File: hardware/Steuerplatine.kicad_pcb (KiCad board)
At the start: 2 copper layers, 110 x 110 mm, 52 parts, among them J1 Conn_01x02_Pin, J2 Conn_01x02_Pin, Q2 BTA16-600B, Q3 BC847BS, U1 LPS28DFW, U2 LNK3202D, U3 Seeed-ESP32C3, U4 TL082

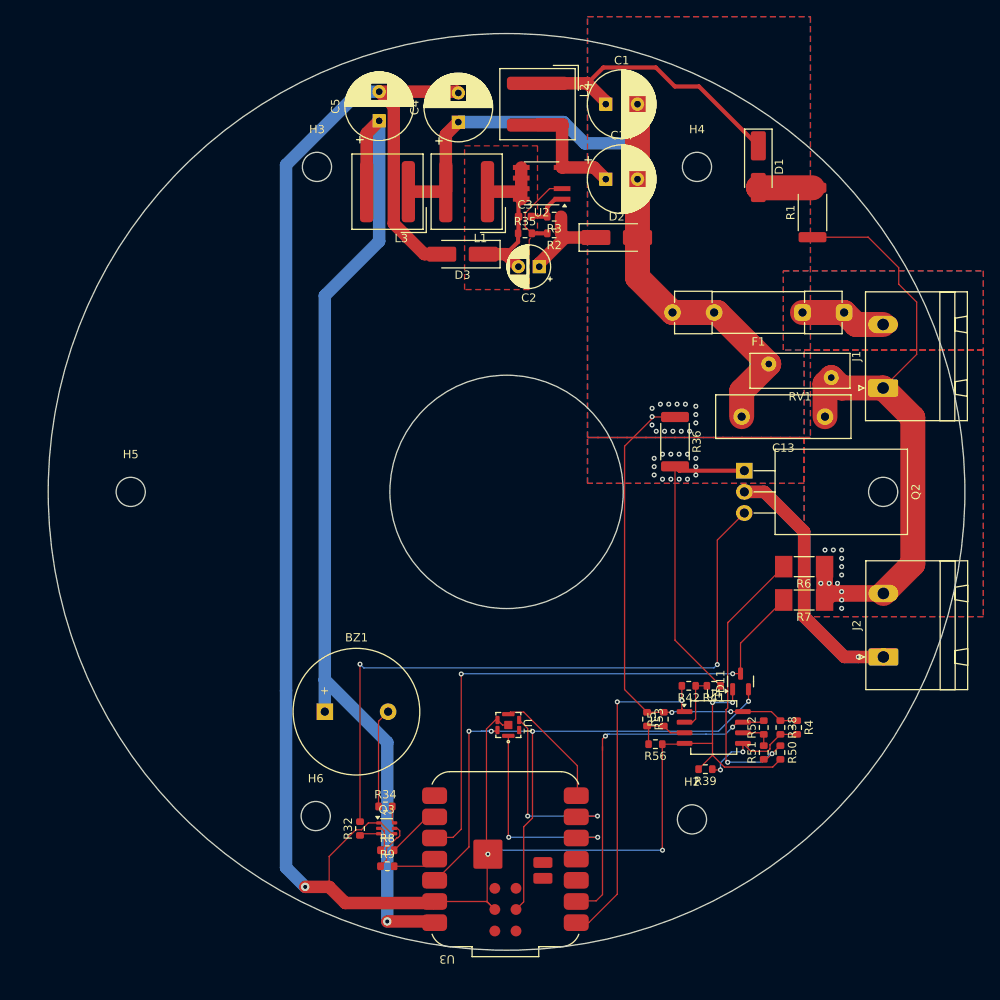
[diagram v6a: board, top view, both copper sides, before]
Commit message: added gnd layer
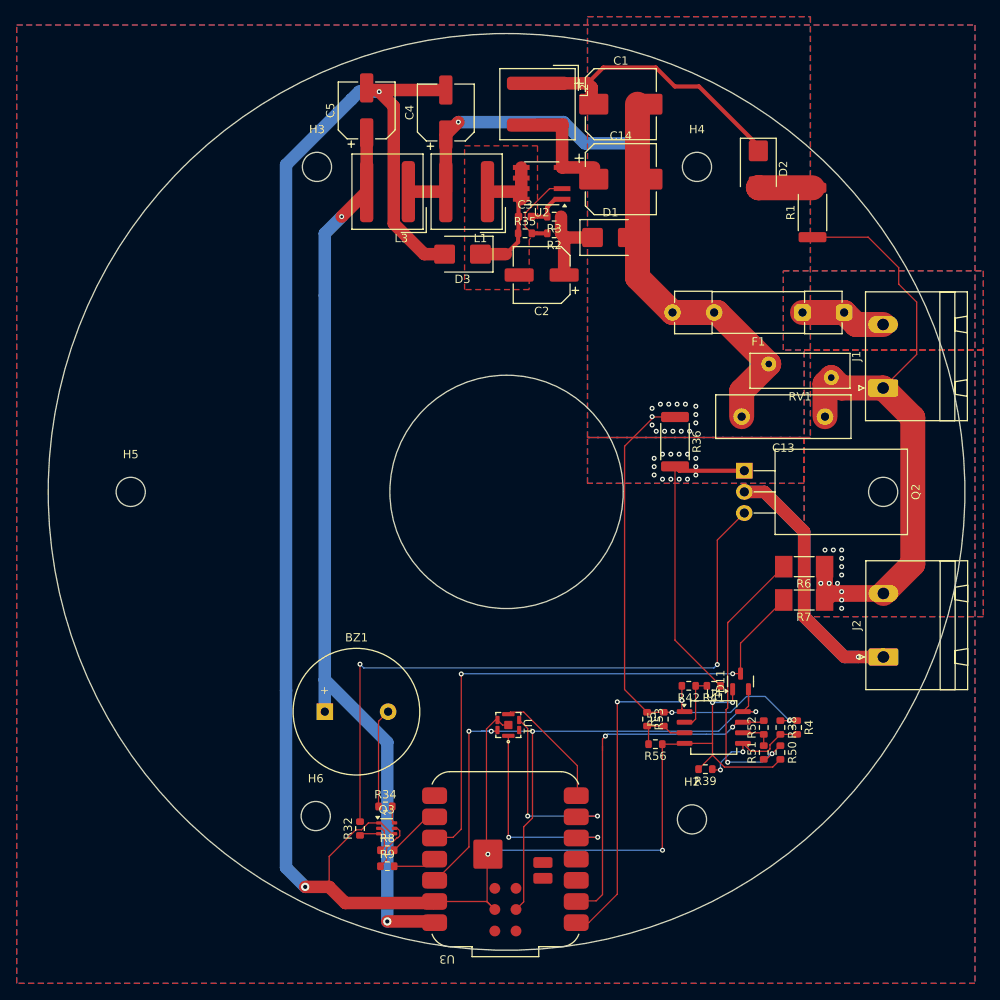
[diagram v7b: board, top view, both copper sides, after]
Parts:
- C1, C14: footprint Capacitor_THT:CP_Radial_D8.0mm_P3.80mm -> Capacitor_SMD:CP_Elec_8x10
- C2: footprint Capacitor_THT:CP_Radial_D5.0mm_P2.50mm -> Capacitor_SMD:CP_Elec_6.3x3
- C4, C5: value 220u -> 22u; footprint Capacitor_THT:CP_Radial_D8.0mm_P3.50mm -> Capacitor_SMD:CP_Elec_6.3x3
- D1: value D -> UF4007; footprint Diode_SMD:D_SMA_Handsoldering -> Diode_SMD:D_SMB
- D2, D3: footprint Diode_SMD:D_SMA_Handsoldering -> Diode_SMD:D_SMB
- moved D1 19.7 mm to (166.2, 110.5), turned to 0 degrees
- moved D2 18.9 mm to (184.0, 102.2), turned to -90 degrees
- moved C5 1.95 mm to (137.0, 95.2)
- moved C4 1.89 mm to (146.5, 95.5)
- moved C1 1.80 mm to (167.5, 94.5)
- moved C14 1.80 mm to (167.5, 103.5)
- moved C2 1.04 mm to (158.0, 115.0)
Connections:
- C1 pad 1: Net-(D1-K) -> Net-(D2-K)
- C2 pad 1: Net-(D2-K) -> Net-(D1-K)
- D1 pad 2: Net-(D1-A) -> /N_filt
- D2 pad 2: /N_filt -> Net-(D2-A)
- L2 pad 1: Net-(D1-K) -> Net-(D2-K)
- R1 pad 2: Net-(D1-A) -> Net-(D2-A)
- R2 pad 1: Net-(D2-K) -> Net-(D1-K)
- R3 pad 1: Net-(D2-K) -> Net-(D1-K)
- U4 pad 8: /N_filt -> /+3V3
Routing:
- net Net-(D1-K): track 35.6 -> 10.9 mm
- net Net-(D2-K): track 11.2 -> 34.9 mm
- net /+5V: track 120.7 -> 109.4 mm, vias 1 -> 2
- net Net-(D2-A): track 0.00 -> 6.52 mm
- net Net-(D1-A): track 6.52 -> 0.00 mm
- net /+3V3: track 80.2 -> 84.1 mm
- net /N_filt: track 155.2 -> 157.9 mm, vias 17 -> 18
- net Net-(D3-K): track 20.2 -> 18.1 mm
- net Net-(U2-D): track 13.9 -> 12.0 mm
- net /GND: vias 5 -> 6
- added copper zone on B.Cu, net /GND
- added copper zone on F.Cu, net /GND

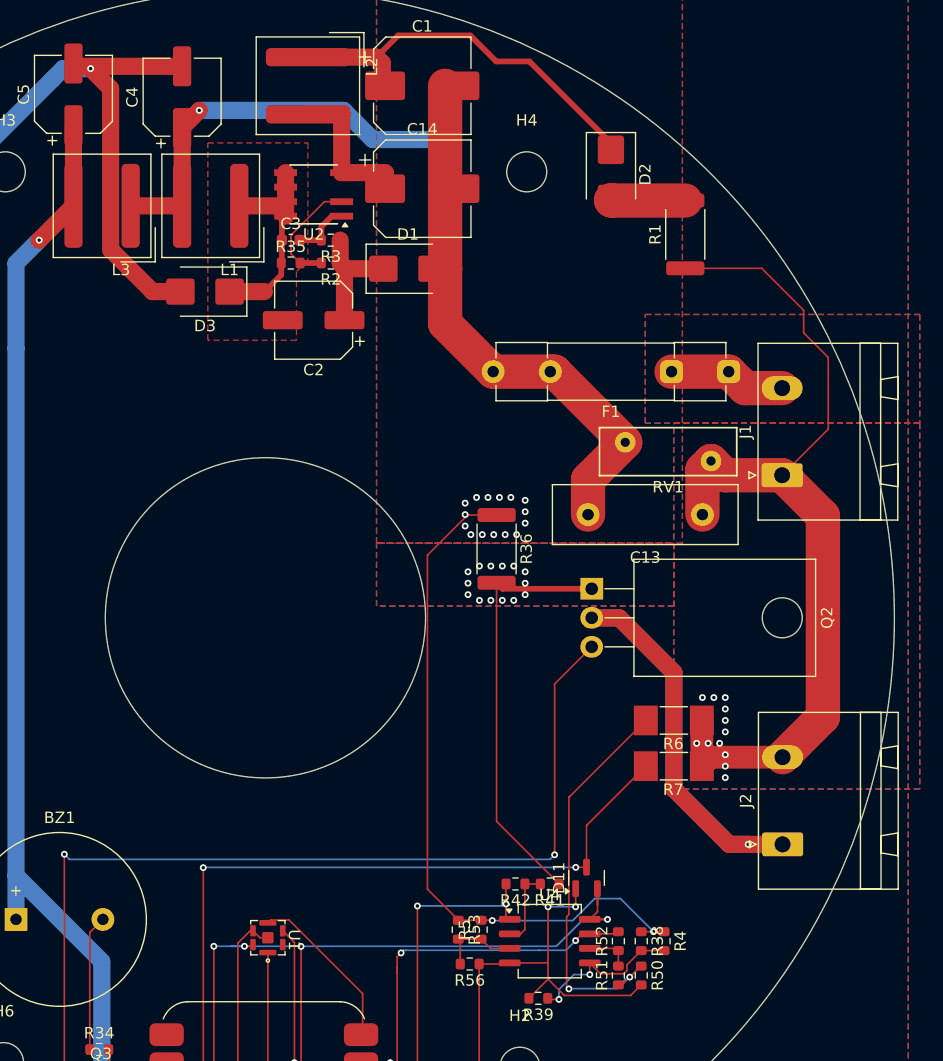
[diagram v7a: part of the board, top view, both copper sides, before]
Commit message: restructured copper planes
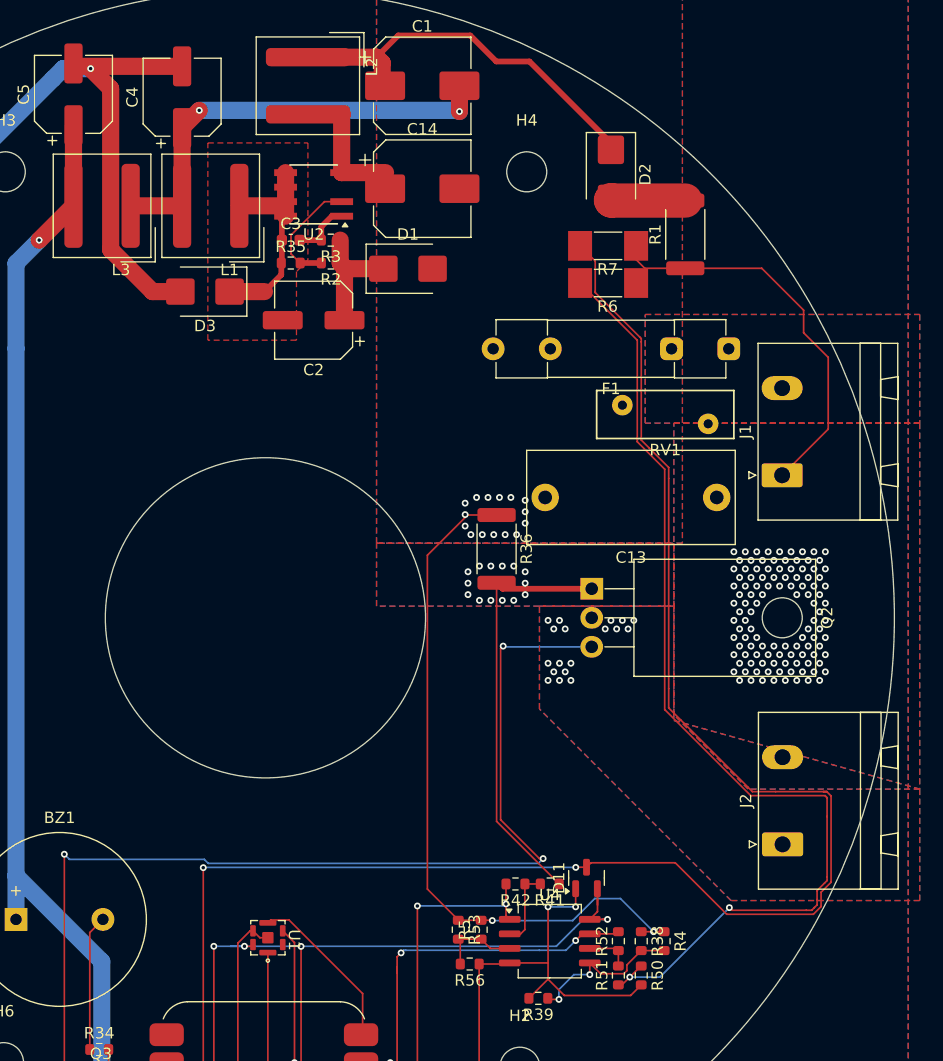
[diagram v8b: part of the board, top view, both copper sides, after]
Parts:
- C13: value 10u -> 1u; footprint Capacitor_THT:C_Disc_D16.0mm_W5.0mm_P10.00mm -> Capacitor_THT:C_Rect_L18.0mm_W8.0mm_P15.00mm_FKS3_FKP3
- moved R7 45.9 mm to (183.8, 108.5)
- moved R6 38.7 mm to (183.8, 111.8)
- moved RV1 3.26 mm to (185.0, 122.4)
- moved F1 2.00 mm to (194.3, 117.5)
- moved C13 1.95 mm to (193.2, 130.5)
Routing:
- net /Controller/ZERO_CROSSING: track 66.6 -> 149.8 mm
- net /Triac/TRIAC_OUTPUT: track 59.0 -> 0.25 mm, vias 1 -> 18
- net /N_filt: track 157.9 -> 100.6 mm, vias 18 -> 19
- net Net-(R50-Pad1): track 35.0 -> 89.5 mm
- net /L: track 79.6 -> 34.7 mm, vias 12 -> 113
- net /N: track 10.3 -> 0.00 mm
- net Net-(Q2-G): track 81.7 -> 89.4 mm, vias 2 -> 3
- added copper zone on B.Cu, net /Triac/TRIAC_OUTPUT
- added copper zone on F.Cu, net /Triac/TRIAC_OUTPUT
